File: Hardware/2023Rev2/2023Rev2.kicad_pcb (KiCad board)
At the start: 2 copper layers, 279.4 x 181.4 mm, 113 parts, among them J1 Conn_01x09, J2 Conn_01x09, J3 Conn_01x04, J4 Conn_01x03, J5 Conn_01x02, J6 Conn_02x03_Counter_Clockwise, J7 RJ45_LED_Shielded, J8 Conn_01x03, Q1 Q_NMOS_GDS, Q2 Q_NMOS_DGS, Q3 Q_NMOS_DGS, Q4 Q_NMOS_DGS, U1 Teensy4.1_DEV-16771, U10 LT1910, U2 BMS_Logic_Switch, U3 Opamp_Dual, U4 ACS758xCB-200B-PFF, U5 Opamp_Dual, U6 OKI, U7 Opamp_Dual, U8 Opamp_Dual, U9 TSR_1-2450

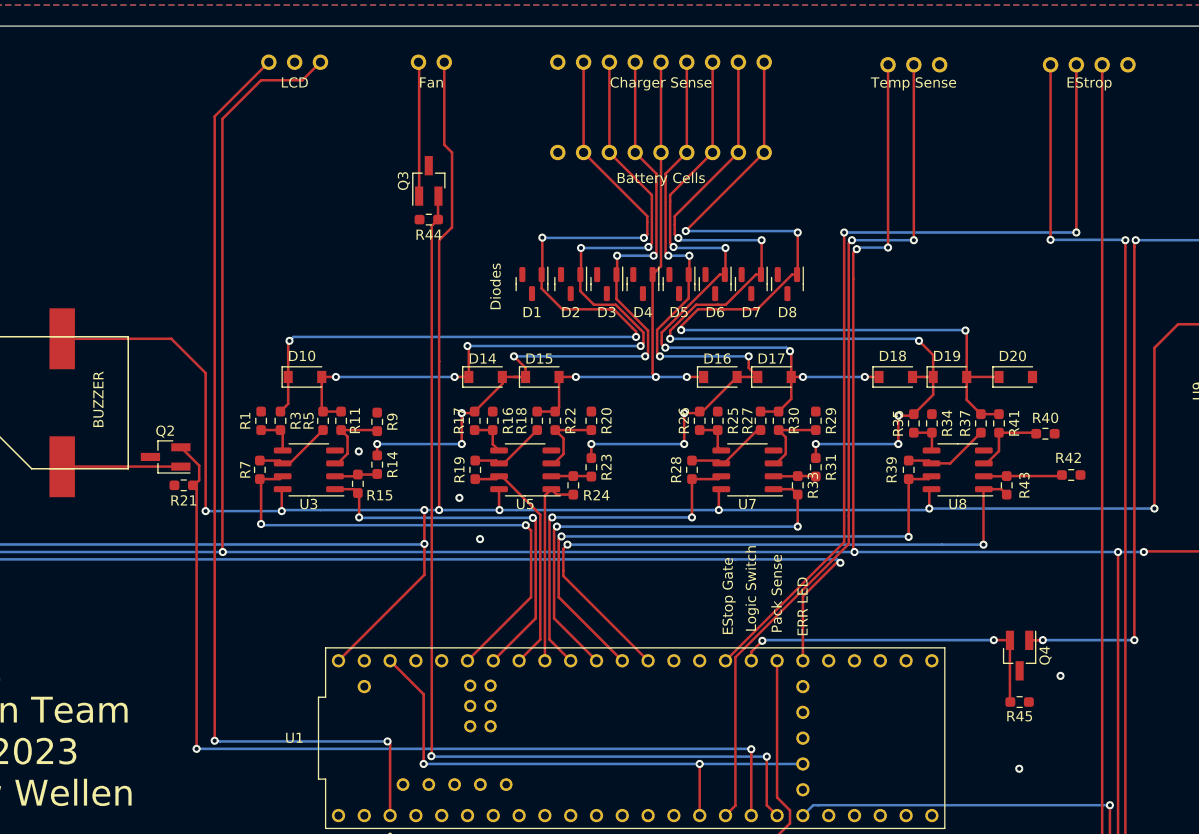
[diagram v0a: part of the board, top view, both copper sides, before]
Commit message: Fixed N-Channel Transistor Footprints and OpAmp supply voltage
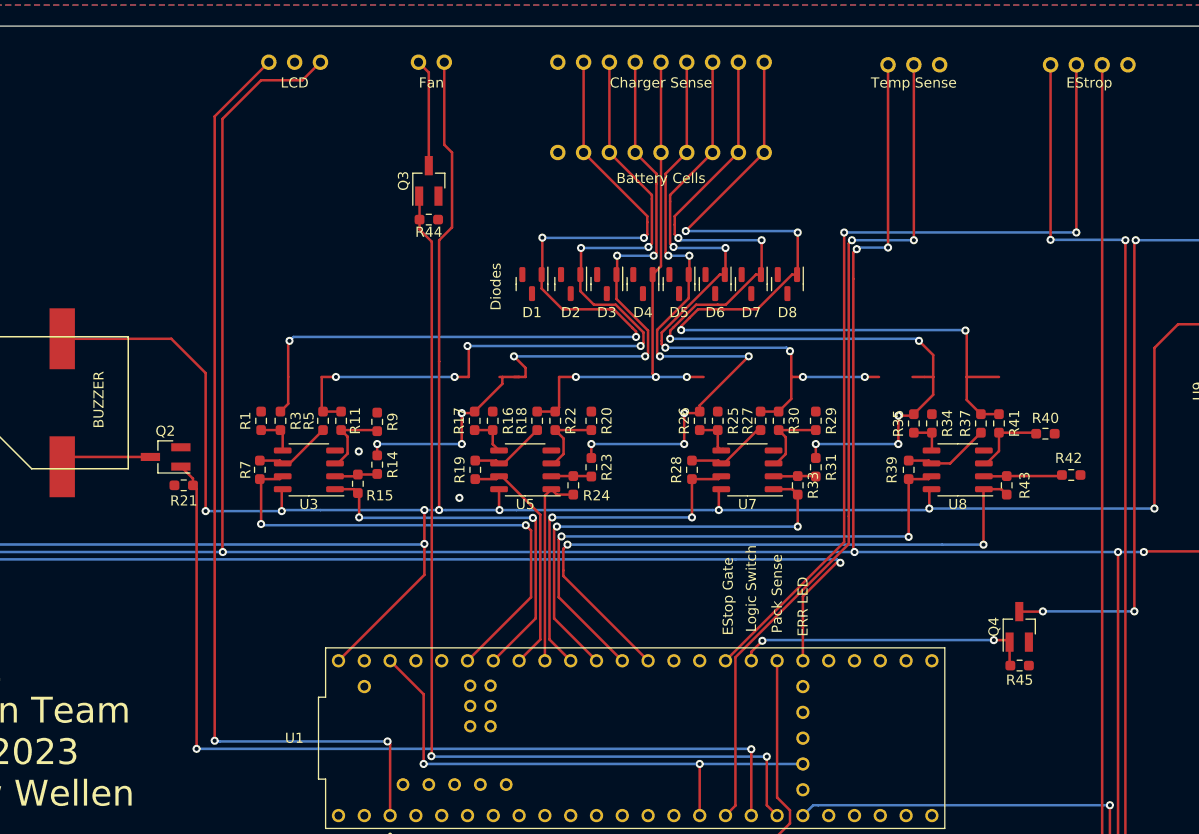
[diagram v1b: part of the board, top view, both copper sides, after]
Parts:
- removed D10, D14, D15, D16, D17, D18, D19, D20: D_Schottky, Diode_SMD:D_SOD-123
- R1, R15, R16, R19, R20, R24, R25, R28, R29, R33, R34, R39, R40, R43, R7, R9: value 32k -> 36.5k
- R11, R14, R17, R18, R22, R23, R26, R27, R3, R30, R31, R35, R37, R41, R42, R5: value 40k -> 46.4k
- moved R45 3.59 mm to (226.9, 101.1)
- moved Q4 2.83 mm to (226.8, 97.3), turned to 90 degrees
- turned R44 to 180 degrees
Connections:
- R33 pad 2: Cell3-SENSE -> unconnected-(R33-Pad2)
- U3 pad 8: +5V -> PACK_OUT
- U5 pad 8: +5V -> PACK_OUT
- U7 pad 8: +5V -> PACK_OUT
- U8 pad 8: +5V -> PACK_OUT
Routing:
- net LOGIC_SWITCH: track 32.9 -> 29.2 mm
- net Net-(BZ1-Pad2): track 11.7 -> 9.08 mm
- net Net-(J5-Pad1): track 13.3 -> 10.8 mm
- net Net-(Q2-Pad2): track 92.1 -> 89.7 mm
- net Net-(Q4-Pad1): track 74.9 -> 72.8 mm
- net cell4: track 67.1 -> 65.0 mm
- net GND: vias 2 -> 0
- net (no net): vias 3 -> 2

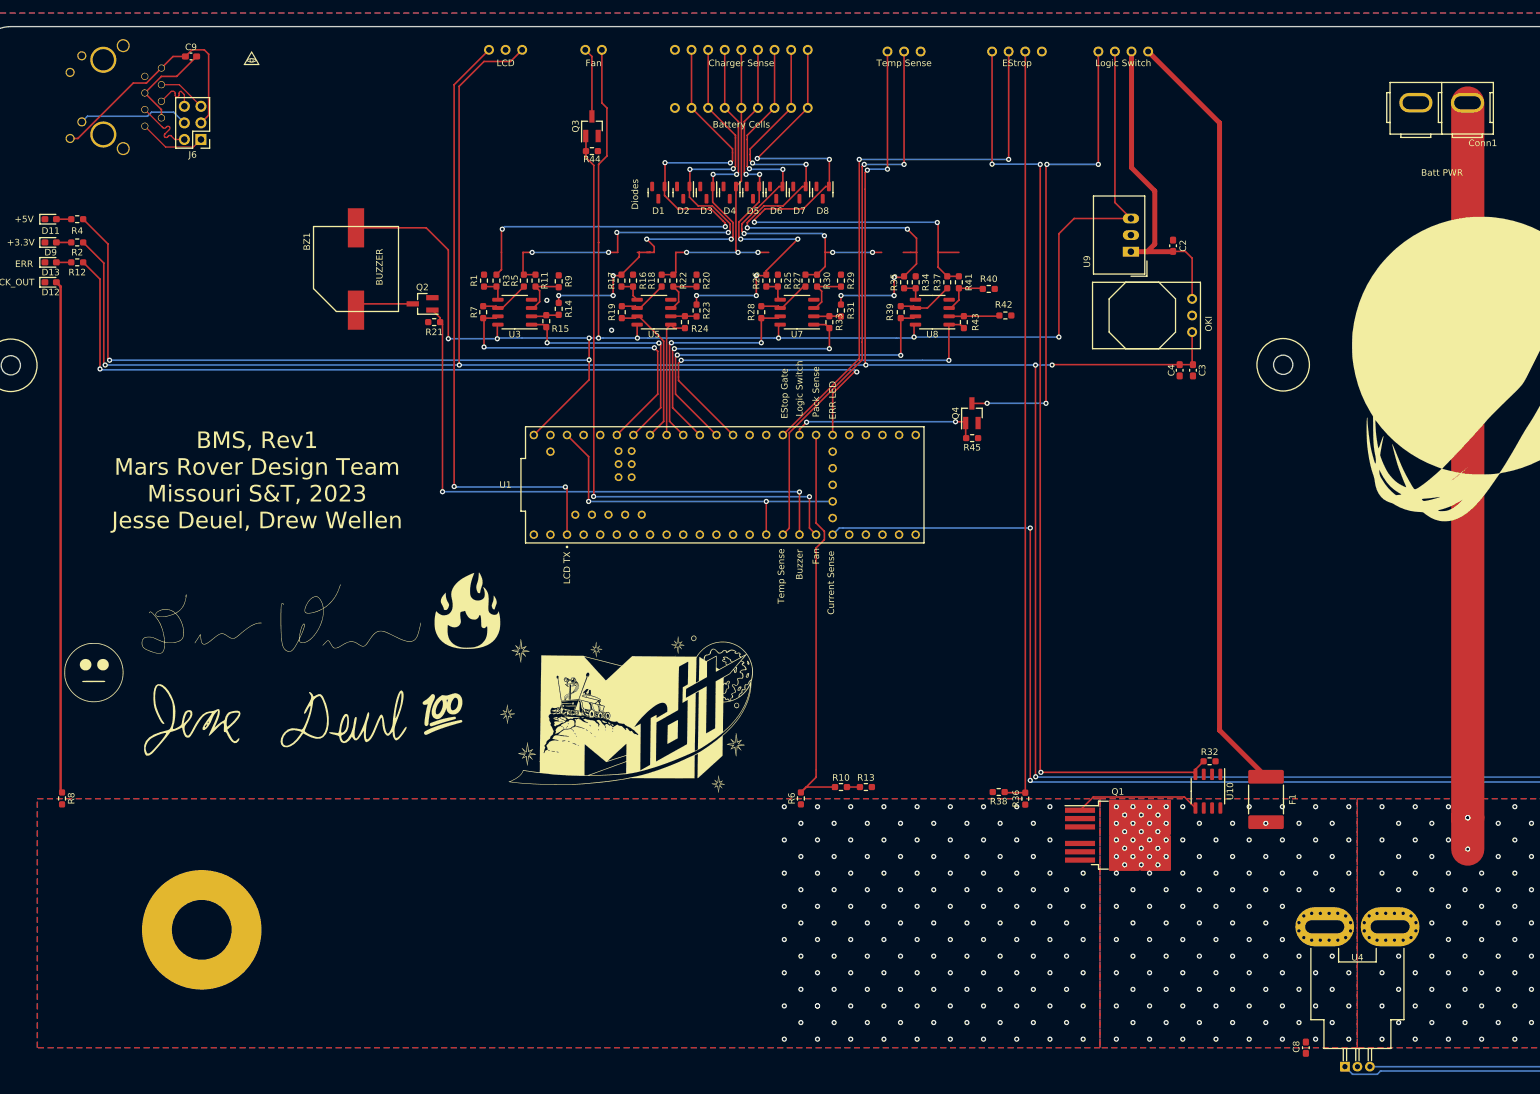
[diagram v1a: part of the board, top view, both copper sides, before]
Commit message: Nearing completion of Rev2 Schematic
Started adding ethernet traces, Fixed resistor values, made Op-amp layouts consistent, and started adding LED indicators.
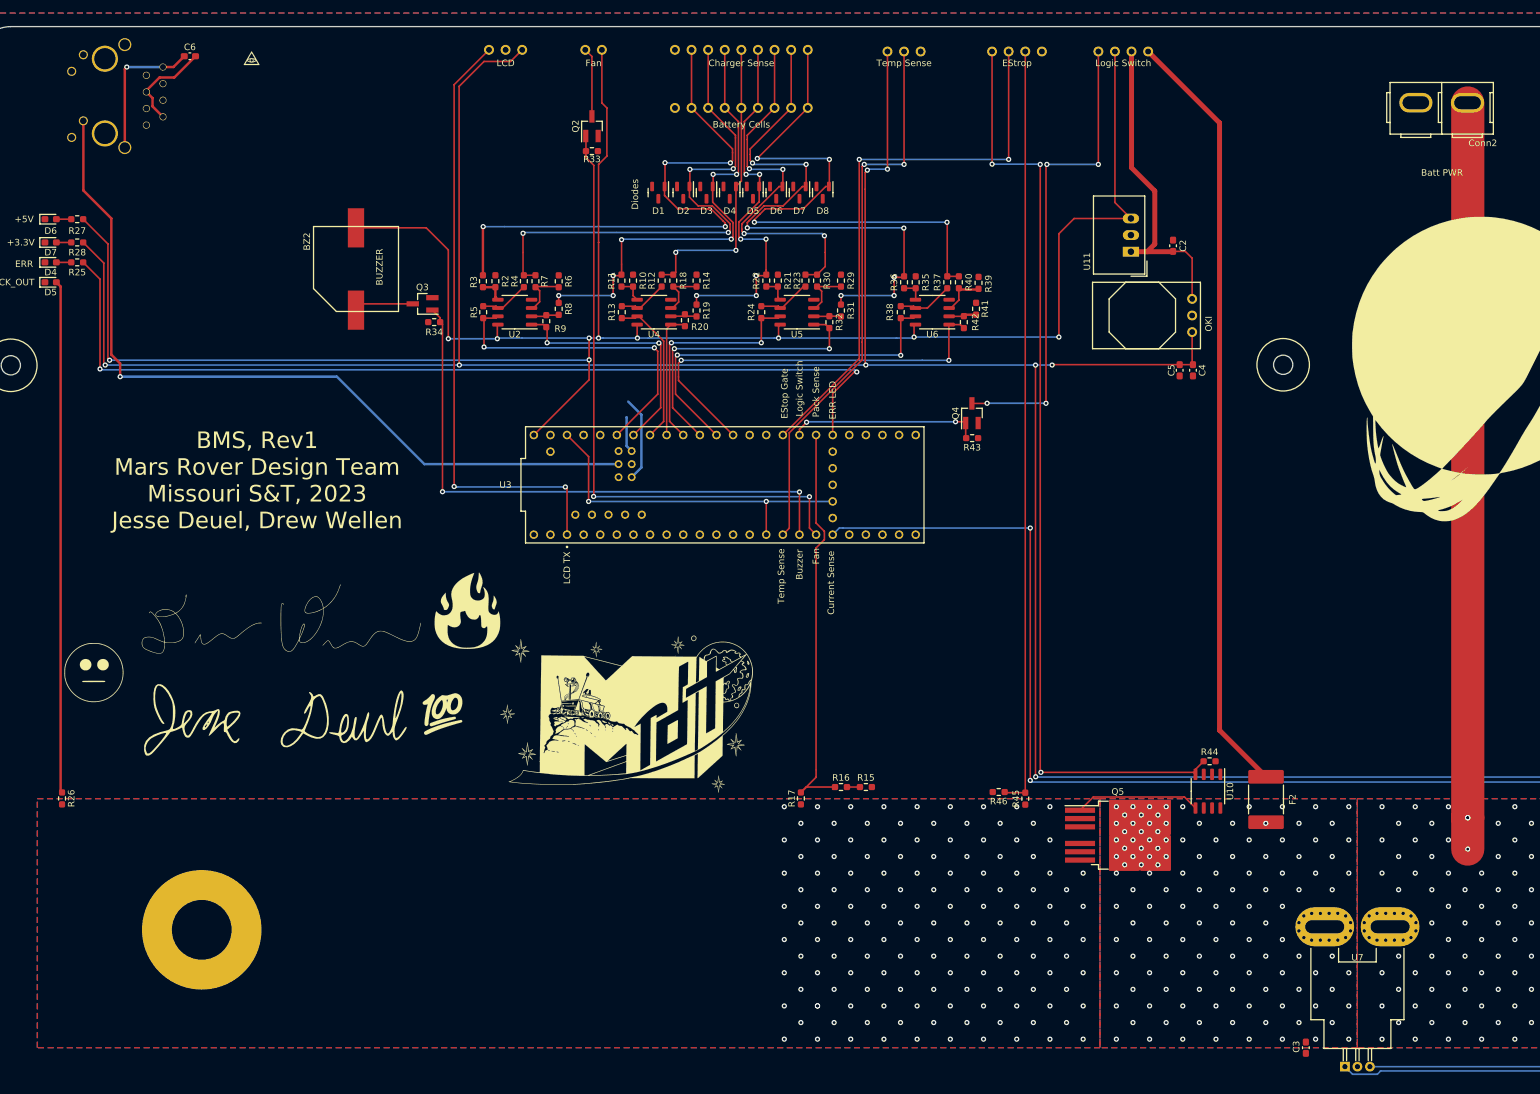
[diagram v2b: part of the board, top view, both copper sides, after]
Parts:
- removed C9: 0.1uF, Capacitor_SMD:C_0603_1608Metric_Pad1.08x0.95mm_HandSolder
- removed the J6 at (108.9, 55.4)
- added C6: 0.1uF, Capacitor_SMD:C_0603_1608Metric_Pad1.08x0.95mm_HandSolder, F.Cu at (107.2, 42.7)
- moved R41 4.60 mm to (227.5, 81.3), turned to -90 degrees
- moved R3 2.07 mm to (152.0, 77.1)
- moved R39 1.81 mm to (227.8, 77.3), turned to 90 degrees
- moved R2 1.74 mm to (153.9, 77.1)
- moved R20 0.29 mm to (182.9, 83.1)
- moved J7 0.29 mm to (81.2, 48.6)
- moved R4 0.09 mm to (158.3, 77.1)
- moved R7 0.09 mm to (160.1, 77.1)
- renumbered BZ1 to BZ2, C8 to C3, C3 to C4, C4 to C5, Conn1 to Conn2, D13 to D4, D12 to D5, D11 to D6, D9 to D7, F1 to F2, H1 to H2, H2 to H3, H3 to H4, H4 to H5, H5 to H6, H6 to H7, J8 to J2, J4 to J3, J5 to J4, J1 to J5, J2 to J6, J3 to J9, Q3 to Q2, Q2 to Q3, Q1 to Q5, R16 to R10, R17 to R11, R18 to R12, R19 to R13, R20 to R14, R13 to R15, R10 to R16, R6 to R17, R22 to R18, R23 to R19, R1 to R2, R24 to R20, R25 to R21, R26 to R22, R27 to R23, R28 to R24, R12 to R25, R8 to R26, R4 to R27, R2 to R28, R33 to R32, R44 to R33, R21 to R34, R34 to R35, R35 to R36, R39 to R38, R40 to R39, R5 to R4, R41 to R40, R42 to R41, R43 to R42, R45 to R43, R32 to R44, R36 to R45, R38 to R46, R7 to R5, R9 to R6, R11 to R7, R14 to R8, R15 to R9, U9 to U11, U3 to U2, U1 to U3, U5 to U4, U7 to U5, U8 to U6, U4 to U7, U2 to U8, U6 to U9, V1 to V2, V2 to V3, V3 to V4
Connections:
- J4 pad 1: Net-(J5-Pad1) -> Net-(D2-Pad2)
- J5 pad 1: GND -> cell8
- J5 pad 2: cell8 -> cell7
- J5 pad 3: cell7 -> call6
- J5 pad 4: call6 -> cell5
- J5 pad 5: cell5 -> cell4
- J5 pad 6: cell4 -> cell3
- J5 pad 7: cell3 -> cell2
- J5 pad 8: cell2 -> cell1
- J5 pad 9: cell1 -> GND
- J6 pad 1: GND -> cell8
- J6 pad 2: cell8 -> cell7
- J6 pad 3: cell7 -> call6
- J6 pad 4: call6 -> cell5
- J6 pad 5: cell5 -> cell4
- J6 pad 6: cell4 -> cell3
- J6 pad 7: cell3 -> cell2
- J6 pad 8: cell2 -> cell1
- J6 pad 9: cell1 -> GND
- J7 pad 1: /Tx+ -> T+
- J7 pad 10: Net-(J6-Pad4) -> LED
- J7 pad 3: /Tx- -> T-
- J7 pad 4: /Rx+ -> R+
- J7 pad 6: /Rx- -> R-
- J7 pad 8: Net-(C9-Pad1) -> GND
- J7 pad 9: Net-(C9-Pad1) -> GND
- Q2 pad 1: Net-(J5-Pad1) -> Net-(D2-Pad1)
- R32 pad 2: unconnected-(R33-Pad2) -> Cell3-SENSE
- U3 pad LED: unconnected-(U1-PadLED) -> LED
- U3 pad R+: unconnected-(U1-PadR+) -> R+
- U3 pad T+: unconnected-(U1-PadT+) -> T+
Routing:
- net LED: track 0.00 -> 123.3 mm, vias 0 -> 1
- net cell7: track 80.2 -> 171.3 mm, vias 6 -> 8
- net cell8: track 88.3 -> 0.00 mm, vias 4 -> 0
- net Net-(C9-Pad1): track 38.1 -> 0.00 mm
- net GND: track 0.00 -> 21.9 mm, vias 0 -> 1
- net Net-(J6-Pad4): track 17.0 -> 0.00 mm
- net T+: track 0.00 -> 13.0 mm
- net Net-(J5-Pad1): track 10.8 -> 0.00 mm
- net Net-(D2-Pad2): track 0.00 -> 10.8 mm
- net /Tx+: track 10.4 -> 0.00 mm
- net /Tx-: track 10.3 -> 0.00 mm
- net cell3: track 67.4 -> 58.8 mm, vias 6 -> 4
- net /Rx-: track 7.42 -> 0.00 mm
- net /Rx+: track 7.37 -> 0.00 mm
- net cell4: track 65.0 -> 58.2 mm
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
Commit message: Finished schematic Rev2
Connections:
- U3 pad R-: (no net) -> R-
- U3 pad T-: (no net) -> T-
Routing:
- net cell7: track 171.3 -> 80.1 mm, vias 8 -> 4
- net cell8: track 0.00 -> 91.2 mm, vias 0 -> 4
- net LED: track 123.3 -> 67.6 mm, vias 1 -> 2
- net T+: track 13.0 -> 0.00 mm
- net (no net): track 5.48 -> 0.00 mm
- net GND: vias 1 -> 6

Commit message: fixed nmos footprint
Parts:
- removed D1: D_Zener, Package_TO_SOT_SMD:SOT-23
- removed the G*** at (149.6, 128.1)
- removed the G*** at (145.8, 143.3)
- removed the G*** at (116.6, 43.0)
- removed the G*** at (316.0, 209.3)
- removed the G*** at (174.0, 143.5)
- removed the G*** at (315.0, 83.8)
- removed the G*** at (92.5, 136.9)
- added D2: Fan, LED_SMD:LED_0603_1608Metric_Pad1.05x0.95mm_HandSolder, F.Cu at (139.7, 54.9)
- added D3: Buzzer, LED_SMD:LED_0603_1608Metric_Pad1.05x0.95mm_HandSolder, F.Cu at (135.3, 57.5)
- added D8: Pack, LED_SMD:LED_0603_1608Metric_Pad1.05x0.95mm_HandSolder, F.Cu at (135.3, 54.9)
- D2: value D_Zener -> Fan; footprint Package_TO_SOT_SMD:SOT-23 -> LED_SMD:LED_0603_1608Metric_Pad1.05x0.95mm_HandSolder
- D3: value D_Zener -> Buzzer; footprint Package_TO_SOT_SMD:SOT-23 -> LED_SMD:LED_0603_1608Metric_Pad1.05x0.95mm_HandSolder
- D4: value D_Zener -> ERR; footprint Package_TO_SOT_SMD:SOT-23 -> LED_SMD:LED_0603_1608Metric_Pad1.05x0.95mm_HandSolder
- D5: value D_Zener -> PACK_OUT; footprint Package_TO_SOT_SMD:SOT-23 -> LED_SMD:LED_0603_1608Metric_Pad1.05x0.95mm_HandSolder
- D6: value D_Zener -> 5V; footprint Package_TO_SOT_SMD:SOT-23 -> LED_SMD:LED_0603_1608Metric_Pad1.05x0.95mm_HandSolder
- D7: value D_Zener -> 3V3; footprint Package_TO_SOT_SMD:SOT-23 -> LED_SMD:LED_0603_1608Metric_Pad1.05x0.95mm_HandSolder
- D8: value D_Zener -> Pack; footprint Package_TO_SOT_SMD:SOT-23 -> LED_SMD:LED_0603_1608Metric_Pad1.05x0.95mm_HandSolder
- moved Q3 0.22 mm to (143.0, 80.5)
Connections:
- D2 pad 1: cell7 -> Net-(D2-Pad1)
- D2 pad 2: GND -> Net-(J4-Pad1)
- D3 pad 1: call6 -> Net-(D3-Pad1)
- D3 pad 2: GND -> Net-(BZ2-Pad2)
- D4 pad 1: cell5 -> GND
- D4 pad 2: GND -> Net-(D4-Pad2)
- D5 pad 1: cell4 -> GND
- D5 pad 2: GND -> Net-(D5-Pad2)
- D6 pad 1: cell3 -> GND
- D6 pad 2: GND -> Net-(D6-Pad2)
- D7 pad 1: cell2 -> GND
- D7 pad 2: GND -> Net-(D7-Pad2)
- D8 pad 1: cell1 -> Net-(D8-Pad1)
- D8 pad 2: GND -> PACK_OUT
- J4 pad 1: Net-(D2-Pad2) -> Net-(J4-Pad1)
- Q2 pad 1: Net-(D2-Pad1) -> Net-(Q2-Pad1)
- Q2 pad 2: Net-(Q2-Pad2) -> GND
- Q2 pad 3: GND -> Net-(J4-Pad1)
- Q3 pad 1: Net-(BZ2-Pad2) -> Net-(Q3-Pad1)
- Q3 pad 2: Net-(Q3-Pad2) -> GND
- Q3 pad 3: GND -> Net-(BZ2-Pad2)
- Q4 pad 1: Net-(Q4-Pad1) -> LOGIC_SWITCH
- Q4 pad 2: LOGIC_SWITCH -> GND
- Q4 pad 3: GND -> Net-(Q4-Pad3)
- Q5 pad 1: Net-(Q5-Pad1) -> Net-(C3-Pad1)
- R33 pad 2: Net-(Q2-Pad2) -> Net-(Q2-Pad1)
- R34 pad 2: Net-(Q3-Pad2) -> Net-(Q3-Pad1)
- U10 pad 5: Net-(Q5-Pad1) -> Net-(C3-Pad1)
- U3 pad 25: Net-(Q3-Pad2) -> Net-(Q3-Pad1)
- U3 pad 26: Net-(Q2-Pad2) -> Net-(Q2-Pad1)
- U3 pad R-: R- -> (no net)
- U3 pad T-: T- -> (no net)
- U8 pad 1: Net-(Q4-Pad1) -> Net-(Q4-Pad3)
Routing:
- net Net-(Q2-Pad1): track 0.00 -> 105.7 mm, vias 0 -> 2
- net Net-(Q2-Pad2): track 94.9 -> 0.00 mm, vias 2 -> 0
- net cell7: track 80.1 -> 171.3 mm, vias 4 -> 8
- net cell8: track 91.2 -> 0.00 mm, vias 4 -> 0
- net Net-(Q3-Pad2): track 89.7 -> 0.00 mm, vias 2 -> 0
- net Net-(Q3-Pad1): track 0.00 -> 89.7 mm, vias 0 -> 2
- net cell1: track 88.5 -> 177.5 mm, vias 4 -> 11
- net Net-(Q4-Pad3): track 0.00 -> 72.8 mm, vias 0 -> 4
- net Net-(Q4-Pad1): track 72.8 -> 0.00 mm, vias 4 -> 0
- net cell3: track 58.8 -> 0.00 mm, vias 4 -> 0
- net cell4: track 58.2 -> 103.9 mm, vias 7 -> 9
- net cell5: track 45.7 -> 0.00 mm, vias 2 -> 0
- net cell2: track 89.0 -> 58.8 mm, vias 7 -> 4
- net Net-(Q5-Pad1): track 19.2 -> 0.00 mm
- net Net-(C3-Pad1): track 0.00 -> 19.2 mm
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
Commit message: Dimensioned Rev2 Layout
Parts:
- removed the D2 at (182.7, 63.5)
- removed the D2 at (139.7, 54.9)
- removed the D3 at (135.3, 57.5)
- removed the D3 at (186.2, 63.5)
- removed the D4 at (189.8, 63.5)
- removed the D4 at (85.9, 74.2)
- removed the D5 at (193.3, 63.5)
- removed the D5 at (85.9, 77.3)
- removed the D6 at (85.9, 67.6)
- removed the D6 at (196.9, 63.5)
- removed the D7 at (85.9, 71.2)
- removed the D7 at (200.4, 63.5)
- removed the D8 at (135.3, 54.9)
- removed the D8 at (204.0, 63.5)
- removed G***: LOGO, Signatures:Drew Signature
- removed G***: LOGO, Signatures:Jesse Signature
- added D2: Fan, LED_SMD:LED_0603_1608Metric_Pad1.05x0.95mm_HandSolder, F.Cu at (29.5, 176.7)
- added D3: Buzzer, LED_SMD:LED_0603_1608Metric_Pad1.05x0.95mm_HandSolder, F.Cu at (43.3, 146.3)
- added D4: ERR, LED_SMD:LED_0603_1608Metric_Pad1.05x0.95mm_HandSolder, F.Cu at (33.9, 174.1)
- added D5: PACK_OUT, LED_SMD:LED_0603_1608Metric_Pad1.05x0.95mm_HandSolder, F.Cu at (43.3, 148.9)
- added D6: 5V, LED_SMD:LED_0603_1608Metric_Pad1.05x0.95mm_HandSolder, F.Cu at (29.5, 174.1)
- added D7: 3V3, LED_SMD:LED_0603_1608Metric_Pad1.05x0.95mm_HandSolder, F.Cu at (45.2, 161.8)
- added D8: Pack, LED_SMD:LED_0603_1608Metric_Pad1.05x0.95mm_HandSolder, F.Cu at (40.8, 161.8)
- J2, J3, J4, J5, J6, J7, J9, U8: moved to F.Cu
- moved Conn2 277.6 mm to (47.6, 167.8)
- moved V2 247.8 mm to (77.3, 139.6)
- moved C4 225.7 mm to (43.3, 151.4), turned to 0 degrees
- moved H6 222.2 mm to (267.9, 96.1)
- moved Q5 219.5 mm to (23.4, 162.9)
- moved H3 216.7 mm to (67.4, 175.5)
- moved F2 210.8 mm to (61.3, 167.8), turned to 0 degrees
- moved U9 203.6 mm to (69.8, 151.1), turned to 0 degrees
- moved C3 200.6 mm to (78.1, 175.7), turned to 0 degrees
- moved R26 196.7 mm to (274.7, 95.2), turned to 0 degrees
- moved J6 190.2 mm to (24.0, 157.4)
- moved Q2 189.0 mm to (24.1, 175.1), turned to 0 degrees
- moved R44 186.4 mm to (78.3, 126.9)
- moved R22 186.1 mm to (38.2, 176.7), turned to 0 degrees
- moved R31 185.2 mm to (46.9, 175.1), turned to 0 degrees
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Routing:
- net +3.3V: track 563.7 -> 0.00 mm, vias 10 -> 0
- net +5V: track 345.4 -> 0.00 mm, vias 10 -> 0
- net CURRENT_SENSE: track 265.6 -> 0.00 mm, vias 4 -> 0
- net cell1: track 177.5 -> 0.00 mm, vias 11 -> 0
- net cell7: track 171.3 -> 0.00 mm, vias 8 -> 0
- net ERR_LED: track 144.8 -> 0.00 mm, vias 2 -> 0
- net Net-(J9-Pad1): track 144.3 -> 0.00 mm, vias 3 -> 0
- net Net-(F2-Pad2): track 118.4 -> 0.00 mm
- net Net-(J9-Pad3): track 116.6 -> 0.00 mm
- net Net-(Conn2-Pad2): track 114.1 -> 0.00 mm, vias 105 -> 0
- net Net-(Q2-Pad1): track 105.7 -> 0.00 mm, vias 2 -> 0
- net cell4: track 103.9 -> 0.00 mm, vias 9 -> 0
- net LCD_TX: track 93.5 -> 0.00 mm, vias 2 -> 0
- net Net-(Q3-Pad1): track 89.7 -> 0.00 mm, vias 2 -> 0
- net GATE: track 86.4 -> 0.00 mm, vias 2 -> 0
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- removed copper zone on B.Cu, net GND
- removed copper zone on F.Cu, net GND
- removed copper zone on B.Cu, net Net-(C3-Pad1)
- removed copper zone on F.Cu, net Net-(C3-Pad1)
- removed copper zone on B.Cu, net Net-(Conn2-Pad2)
- removed copper zone on F.Cu, net Net-(Conn2-Pad2)
- removed copper zone on B.Cu, net PACK_OUT
- removed copper zone on F.Cu, net PACK_OUT
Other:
- board outline removed
- board text removed: "+3.3V"
- board text removed: "+5V"
- board text removed: "BATT PWR"
- board text removed: "BMS, Rev1 Mars Rover Design Team Missouri S&T, 2023 Jesse Deuel, Drew Wellen"
- board text removed: "Batt PWR"
- board text removed: "Battery Cells"
- board text removed: "Buzzer"
- board text removed: "Charger Sense"
- board text removed: "Current Sense"
- board text removed: "Diodes"
- board text removed: "ERR"
- board text removed: "ERR LED"
- board text removed: "EStop Gate"
- board text removed: "EStrop"
- board text removed: "Fan"
- board text removed: "GND"
- board text removed: "LCD"
- board text removed: "LCD TX"
- board text removed: "Logic Switch"
- board text removed: "PACK_OUT"
- board text removed: "Pack Sense"
- board text removed: "Temp Sense"
